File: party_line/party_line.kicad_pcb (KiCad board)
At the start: 4 copper layers, 2.2 x 9.2 mm, 39 parts, among them J1 PartyLineIn, J2 PartyLineOut, J3 ExtIn, J4 Headset, SW1 SW_SPDT, SW2 SW_SPDT, U1 NE5532DR, U2 LM386G-S08-R

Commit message: layout
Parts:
- removed C8: 47u, Capacitor_SMD:C_Elec_6.3x5.4
- moved R7 112.2 mm to (156.8, 99.1)
- moved C4 111.5 mm to (156.8, 77.5)
- moved R2 110.8 mm to (159.5, 87.9), turned to -90 degrees
- moved RV2 109.1 mm to (143.6, 65.5), turned to 0 degrees
- moved C1 105.7 mm to (144.1, 87.6), turned to 0 degrees
- moved R1 101.7 mm to (147.3, 94.0), turned to 0 degrees
- moved R5 101.4 mm to (156.8, 108.6)
- moved C2 100.7 mm to (165.7, 102.9)
- moved R3 99.7 mm to (151.1, 80.6), turned to -90 degrees
- moved R6 97.6 mm to (156.8, 103.5)
- moved C9 97.1 mm to (167.0, 79.4), turned to 180 degrees
- moved SW2 92.3 mm to (129.2, 70.6), turned to 180 degrees
- moved R11 91.7 mm to (148.2, 69.6)
- moved C10 91.5 mm to (167.0, 69.2), turned to 180 degrees
- moved R4 87.3 mm to (141.5, 80.6), turned to 0 degrees
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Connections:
- C7 pad 1: PIn_A -> Net-(SW2-B)
- C7 pad 2: Net-(SW2-C) -> Net-(C7-Pad2)
- C9 pad 2: Net-(SW2-B) -> Net-(C7-Pad2)
- R15 pad 1: Out_R -> Out_L
- R16 pad 1: Out_L -> Out_R
- RV2 pad 1: Net-(SW2-B) -> Net-(C7-Pad2)
- SW2 pad 1: Net-(SW2-A) -> PIn_B
- SW2 pad 3: Net-(SW2-C) -> PIn_A
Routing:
- net +12V: track 0.00 -> 138.4 mm, vias 0 -> 4
- net IBus: track 0.00 -> 112.9 mm, vias 0 -> 2
- net PBus: track 0.00 -> 83.5 mm, vias 0 -> 2
- net Net-(SW1-B): track 0.00 -> 61.4 mm
- net Net-(C3-Pad2): track 0.00 -> 60.0 mm, vias 0 -> 2
- net PIn_A: track 0.00 -> 52.7 mm, vias 0 -> 1
- net Net-(U2-+): track 0.00 -> 47.4 mm, vias 0 -> 2
- net PIn_B: track 0.00 -> 41.3 mm, vias 0 -> 1
- net GND: track 0.00 -> 39.4 mm, vias 0 -> 21
- net Net-(C7-Pad2): track 0.00 -> 37.0 mm
- net VBias: track 0.00 -> 36.7 mm
- net Mic: track 0.00 -> 28.6 mm
- net Net-(C12-Pad2): track 0.00 -> 27.6 mm, vias 0 -> 2
- net Out_L: track 0.00 -> 25.9 mm
- net Out_R: track 0.00 -> 24.0 mm
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- added copper zone on In1.Cu, net GND
- added copper zone on In2.Cu, net VCC
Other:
- board size 2.2 x 9.2 mm -> 85.1 x 50.8 mm

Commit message: .
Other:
- board text added: "ERMIS Party Line System 1.0 Design: Spiros Makris S/N:"
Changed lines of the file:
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@@
 		(layer "Edge.Cuts")
+	)
+	(gr_text "ERMIS Party Line System\n1.0\nDesign: Spiros Makris\nS/N:"
+		(at 92.964 77.724 0)
+		(layer "F.SilkS")
+		(effects
+			(font
+				(size 1 1)
+				(thickness 0.15)
+			)
+			(justify left bottom)
+		)
 	)
 	(segment

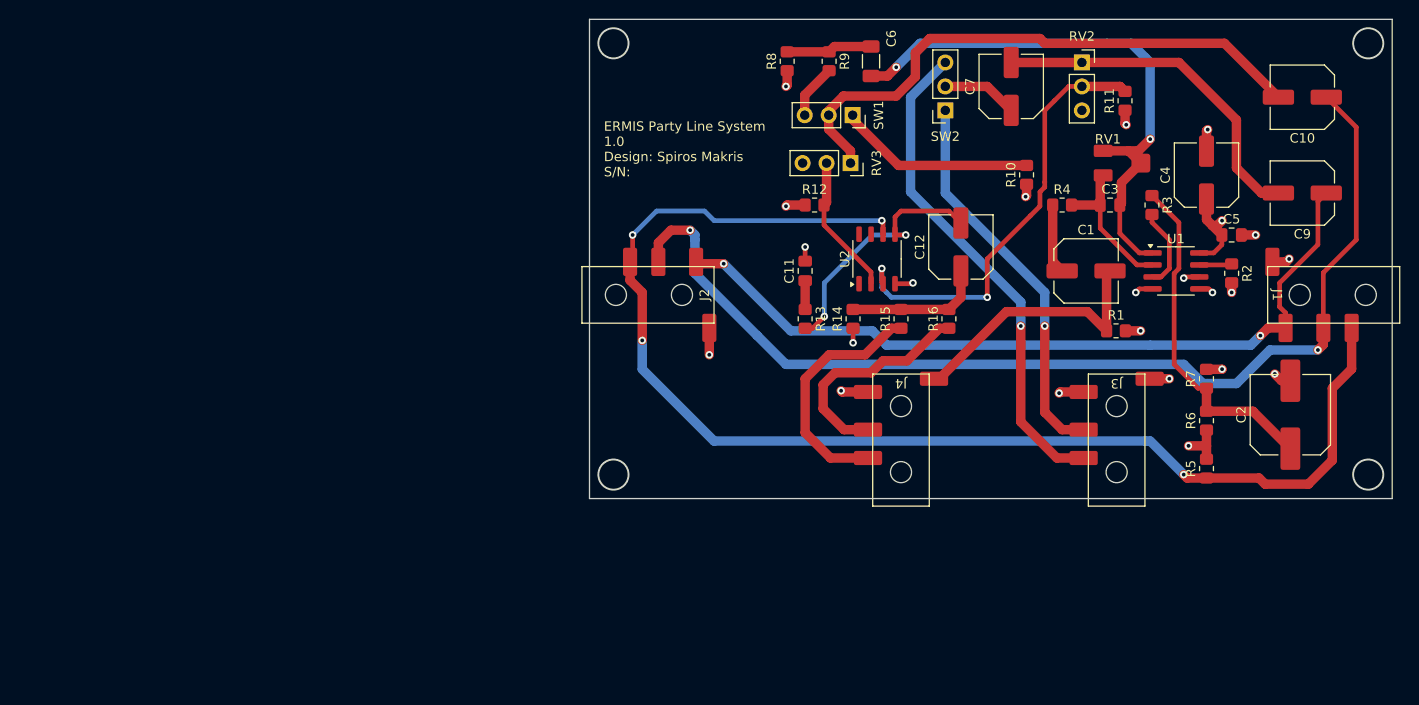
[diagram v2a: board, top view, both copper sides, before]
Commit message: reposition jacks
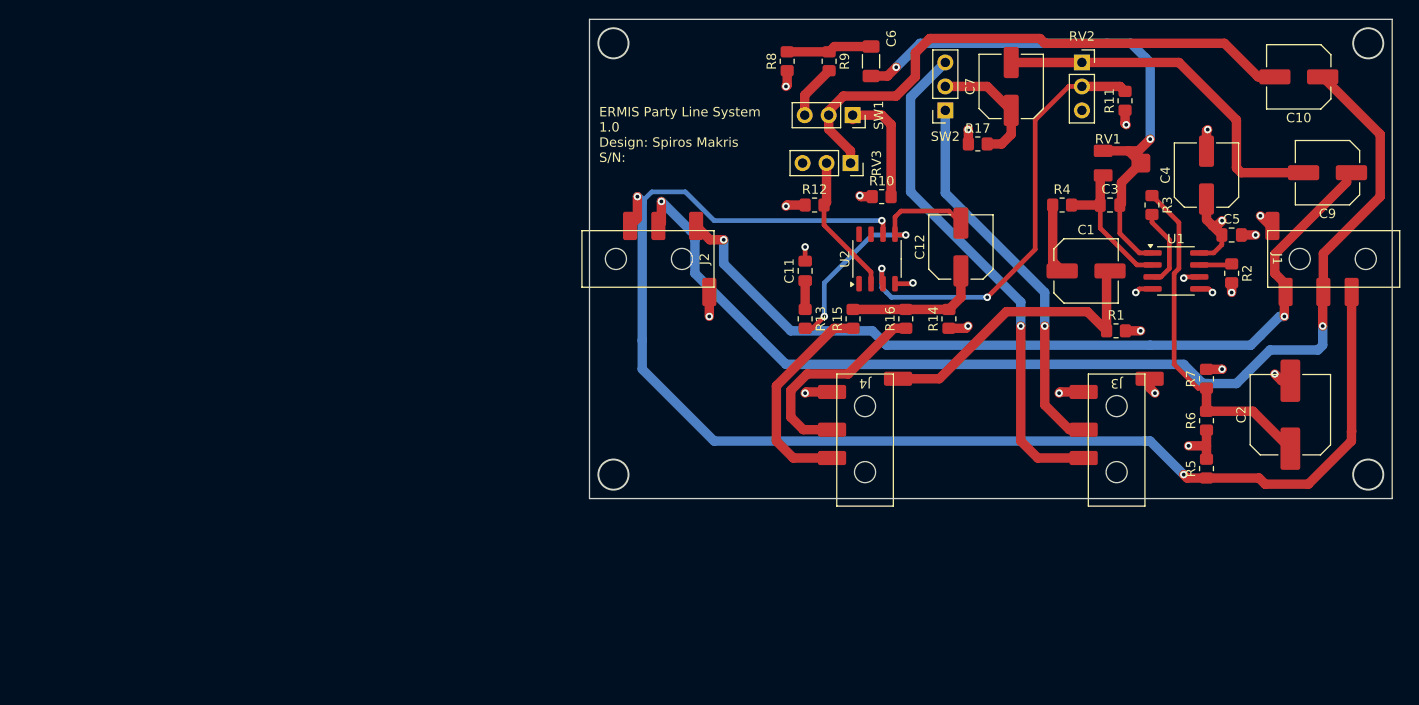
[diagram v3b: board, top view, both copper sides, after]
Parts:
- added R17: 56k, Resistor_SMD:R_0805_2012Metric_Pad1.20x1.40mm_HandSolder, F.Cu at (132.6, 74.2)
- moved R10 15.5 mm to (122.4, 79.8), turned to 0 degrees
- moved R14 10.2 mm to (129.5, 92.7)
- moved R15 5.08 mm to (119.4, 92.7)
- moved R16 4.57 mm to (125.0, 92.7)
- moved J1 3.81 mm to (163.8, 86.4)
- moved J2 3.81 mm to (104.1, 86.4)
- moved J4 3.81 mm to (120.7, 99.1)
- moved C9 3.43 mm to (169.7, 77.2)
- moved C10 2.19 mm to (166.6, 67.1)
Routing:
- net +12V: track 138.4 -> 148.4 mm, vias 4 -> 3
- net Net-(SW1-A): track 20.9 -> 12.6 mm
- net PBus: track 83.5 -> 89.5 mm
- net IBus: track 112.9 -> 118.4 mm
- net Net-(SW2-B): track 8.04 -> 13.5 mm
- net Mic: track 28.6 -> 32.4 mm
- net Out_L: track 25.9 -> 23.1 mm
- net Net-(C7-Pad2): track 37.0 -> 38.8 mm
- net Out_R: track 24.0 -> 22.7 mm
- net GND: track 39.4 -> 40.8 mm, vias 21 -> 22
- net Net-(SW1-B): track 61.4 -> 60.1 mm
- net PIn_A: track 52.7 -> 53.9 mm

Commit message: .
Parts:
- C4: footprint Capacitor_SMD:C_Elec_6.3x5.4 -> Capacitor_SMD:C_Elec_6.3x7.7
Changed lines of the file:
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@@
 			)
 		)
-		(property "Description" "Unpolarized capacitor"
+		(property "Description" "C1798"
 			(at 0 0 0)
 			(layer "F.Fab")
@@
 		(fp_circle
 			(center 0 -2.9)
-			(end 1.118034 -2.9)
+			(end 0.6 -2.9)
 			(stroke
 				(width 0.05)
@@
 		(fp_circle
 			(center 0 -9.9)
-			(end 1.118034 -9.9)
+			(end 0.6 -9.9)
 			(stroke
 				(width 0.05)
@@
 		)
 		(embedded_fonts no)
+		(model "${KIPRJMOD}/3D models/PJ320D.STEP"
+			(offset
+				(xyz -0.3 6.1 -11.5)
+			)
+			(scale
+				(xyz 1 1 1)
+			)
+			(rotate
+				(xyz -0 -0 90)
+			)
+		)
 	)
 	(footprint "Resistor_SMD:R_0805_2012Metric_Pad1.20x1.40mm_HandSolder"
@@
 		)
 	)
-	(footprint "Capacitor_SMD:C_Elec_6.3x5.4"
+	(footprint "Capacitor_SMD:C_Elec_6.3x7.7"
 		(layer "F.Cu")
 		(at 156.845 77.47 90)
-		(descr "SMD capacitor, aluminum electrolytic nonpolar, 6.3x5.4mm")
+		(descr "SMD capacitor, aluminum electrolytic nonpolar, 6.3x7.7mm")
 		(tags "capacitor electrolytic nonpolar")
 		(property "Reference" "C4"
@@
 			)
 		)
+		(property "LCSC" "C3339"
+			(at 0 0 0)
+			(layer "F.SilkS")
+			(hide yes)
+			(effects
+				(font
+					(size 1.27 1.27)
+					(thickness 0.15)
+				)
+			)
+		)
 		(property ki_fp_filters "C_*")
 		(sheetname "/")
@@
 		)
 		(embedded_fonts no)
-		(model "${KICAD9_3DMODEL_DIR}/Capacitor_SMD.3dshapes/C_Elec_6.3x5.4.step"
+		(model "${KICAD9_3DMODEL_DIR}/Capacitor_SMD.3dshapes/C_Elec_6.3x7.7.step"
 			(offset
 				(xyz 0 0 0)
@@
 		(fp_circle
 			(center 0 -2.9)
-			(end 1.118034 -2.9)
+			(end 0.6 -2.9)
 			(stroke
 				(width 0.05)
@@
 		(fp_circle
 			(center 0 -9.9)
-			(end 1.118034 -9.9)
+			(end 0.6 -9.9)
 			(stroke
 				(width 0.05)
@@
 		)
 		(embedded_fonts no)
+		(model "${KIPRJMOD}/3D models/PJ320D.STEP"
+			(offset
+				(xyz -0.3 6.1 -11.5)
+			)
+			(scale
+				(xyz 1 1 1)
+			)
+			(rotate
+				(xyz -0 -0 90)
+			)
+		)
 	)
 	(footprint "Resistor_SMD:R_0805_2012Metric_Pad1.20x1.40mm_HandSolder"
@@
 		(fp_circle
 			(center 0 -9.9)
-			(end 1.118034 -9.9)
+			(end 0.6 -9.9)
 			(stroke
 				(width 0.05)
@@
 		(fp_circle
 			(center 0 -2.9)
-			(end 1.118034 -2.9)
+			(end 0.6 -2.9)
 			(stroke
 				(width 0.05)
@@
 		)
 		(embedded_fonts no)
+		(model "${KIPRJMOD}/3D models/PJ320D.STEP"
+			(offset
+				(xyz -0.3 6.1 -11.5)
+			)
+			(scale
+				(xyz 1 1 1)
+			)
+			(rotate
+				(xyz -0 -0 90)
+			)
+		)
 	)
 	(footprint "custom:3314J-1"
@@
 		(fp_circle
 			(center 0 -2.9)
-			(end 1.118034 -2.9)
+			(end 0.6 -2.9)
 			(stroke
 				(width 0.05)
@@
 		(fp_circle
 			(center 0 -9.9)
-			(end 1.118034 -9.9)
+			(end 0.6 -9.9)
 			(stroke
 				(width 0.05)
@@
 		)
 		(embedded_fonts no)
+		(model "${KIPRJMOD}/3D models/PJ320D.STEP"
+			(offset
+				(xyz -0.3 6.1 -11.5)
+			)
+			(scale
+				(xyz 1 1 1)
+			)
+			(rotate
+				(xyz -0 -0 90)
+			)
+		)
 	)
 	(footprint "Package_SO:SOIC-8_3.9x4.9mm_P1.27mm"
@@
 		)
 	)
+	(dimension
+		(type orthogonal)
+		(layer "F.Cu")
+		(pts
+			(xy 147.32 108.96) (xy 120.65 108.96)
+		)
+		(height 8.388)
+		(orientation 0)
+		(format
+			(prefix "")
+			(suffix "")
+			(units 3)
+			(units_format 0)
+			(precision 4)
+			(suppress_zeroes yes)
+		)
+		(style
+			(thickness 0.2)
+			(arrow_length 1.27)
+			(text_position_mode 0)
+			(arrow_direction outward)
+			(extension_height 0.58642)
+			(extension_offset 0.5)
+			(keep_text_aligned yes)
+		)
+		(gr_text "26.67"
+			(at 133.985 115.548 0)
+			(layer "F.Cu")
+			(effects
+				(font
+					(size 1.5 1.5)
+					(thickness 0.3)
+				)
+			)
+		)
+	)
+	(dimension
+		(type orthogonal)
+		(layer "F.Cu")
+		(pts
+			(xy 173.99 109.22) (xy 147.32 108.97)
+		)
+		(height 8.128)
+		(orientation 0)
+		(format
+			(prefix "")
+			(suffix "")
+			(units 3)
+			(units_format 0)
+			(precision 4)
+			(suppress_zeroes yes)
+		)
+		(style
+			(thickness 0.2)
+			(arrow_length 1.27)
+			(text_position_mode 0)
+			(arrow_direction outward)
+			(extension_height 0.58642)
+			(extension_offset 0.5)
+			(keep_text_aligned yes)
+		)
+		(gr_text "26.67"
+			(at 160.655 115.548 0)
+			(layer "F.Cu")
+			(effects
+				(font
+					(size 1.5 1.5)
+					(thickness 0.3)
+				)
+			)
+		)
+	)
